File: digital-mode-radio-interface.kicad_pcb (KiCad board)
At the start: 2 copper layers, 9 parts, among them U1 FE1.1s, U2 CH340E, U3 CRE1S0505S3C, U4 PC817, U5 PC817, U6 PC817, U7 PC817

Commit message: WIP checkin of PCB layout
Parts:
- added C1: 475, Capacitor_SMD:C_0201_0603Metric, F.Cu at (89.9, 87.0)
- added C10: 475, Capacitor_SMD:C_0201_0603Metric, F.Cu at (112.8, 115.8)
- added C11: 100n, Capacitor_SMD:C_0201_0603Metric, F.Cu at (53.4, 96.7)
- added C12: 100n, Capacitor_SMD:C_0201_0603Metric, F.Cu at (69.1, 95.5)
- added C13: 4.7u, Capacitor_SMD:C_0201_0603Metric, F.Cu at (70.7, 104.0)
- added C14: 100n, Capacitor_SMD:C_0201_0603Metric, F.Cu at (71.4, 99.9)
- added C15: 4.7u, Capacitor_SMD:C_0201_0603Metric, F.Cu at (70.0, 107.1)
- added C16: 10uF, Capacitor_SMD:C_0201_0603Metric, F.Cu at (42.0, 100.5)
- added C18: 101, Capacitor_SMD:C_0201_0603Metric, F.Cu at (51.9, 106.9)
- added C19: 100n, Capacitor_SMD:C_0201_0603Metric, F.Cu at (69.1, 97.6)
- added C2: 10uF, Capacitor_SMD:C_0201_0603Metric, F.Cu at (89.9, 88.5)
- added C3: 10uF, Capacitor_SMD:C_0201_0603Metric, F.Cu at (55.8, 91.7)
- added C4: 10uF, Capacitor_SMD:C_0201_0603Metric, F.Cu at (44.8, 99.0)
- added C5: 475, Capacitor_SMD:C_0201_0603Metric, F.Cu at (40.7, 87.7)
- added C6: 475, Capacitor_SMD:C_0201_0603Metric, F.Cu at (86.5, 113.2)
- added C7: 10uF, Capacitor_SMD:C_0201_0603Metric, F.Cu at (96.3, 117.3)
- added C8: 475, Capacitor_SMD:C_0201_0603Metric, F.Cu at (125.6, 109.8)
- added C9: 475, Capacitor_SMD:C_0201_0603Metric, F.Cu at (121.8, 118.6)
- added D3: YELLOW, LED_SMD:LED_0201_0603Metric, F.Cu at (55.5, 111.7)
- added D4: RED, LED_SMD:LED_0201_0603Metric, F.Cu at (80.2, 94.3)
- added D5: LED, LED_SMD:LED_0201_0603Metric, F.Cu at (34.8, 107.0)
- added J1: Conn_01x09_Socket, Connector_Dsub:DSUB-9_Female_Horizontal_P2.77x2.84mm_EdgePinOffset4.94mm_Housed_MountingHolesOffset7.48mm, F.Cu at (133.8, 96.4)
- added J2: Conn_01x02, Connector_PinHeader_1.00mm:PinHeader_1x02_P1.00mm_Vertical, F.Cu at (108.1, 97.5)
- added J3: Conn_01x03_Pin, Connector_PinHeader_1.00mm:PinHeader_1x03_P1.00mm_Vertical, F.Cu at (59.7, 110.0)
- added L1: 10uH, Inductor_SMD:L_CommonModeChoke_Coilcraft_0805USB, F.Cu at (31.7, 94.3)
- added P1: USB_C_Plug, Connector_USB:USB_C_Receptacle_GCT_USB4085, F.Cu at (32.5, 99.0)
- added Q1: Q_NPN_BCE, Package_TO_SOT_SMD:SOT-23-3, F.Cu at (100.0, 99.7)
- added Q2: Q_NPN_BCE, Package_TO_SOT_SMD:SOT-23-3, F.Cu at (102.3, 108.1)
- added Q3: Q_NPN_BCE, Package_TO_SOT_SMD:SOT-23-3, F.Cu at (99.0, 87.4)
- added Q4: Q_NPN_BCE, Package_TO_SOT_SMD:SOT-23-3, F.Cu at (93.7, 112.4)
- added R1: 1K, Resistor_SMD:R_0201_0603Metric, F.Cu at (65.4, 83.7)
- added R10: 47k, Resistor_SMD:R_0201_0603Metric, F.Cu at (89.5, 112.7)
- added R11: 510, Resistor_SMD:R_0201_0603Metric, F.Cu at (86.6, 118.7)
- added R12: 10k, Resistor_SMD:R_0201_0603Metric, F.Cu at (89.7, 108.4)
- added R13: 33k, Resistor_SMD:R_0201_0603Metric, F.Cu at (93.7, 93.9)
- added R14: 10k, Resistor_SMD:R_0201_0603Metric, F.Cu at (93.9, 85.3)
- added R15: 330, Resistor_SMD:R_0201_0603Metric, F.Cu at (55.8, 108.8)
- added R16: 330, Resistor_SMD:R_0201_0603Metric, F.Cu at (80.2, 95.5)
- added R17: 22, Resistor_SMD:R_0201_0603Metric, F.Cu at (53.0, 93.1)
- added R18: 22, Resistor_SMD:R_0201_0603Metric, F.Cu at (51.8, 108.2)
- added R19: 2.7k, Resistor_SMD:R_0201_0603Metric, F.Cu at (47.2, 104.7)
- added R2: 1K, Resistor_SMD:R_0201_0603Metric, F.Cu at (35.6, 91.4)
- added R20: 2.7k, Resistor_SMD:R_0201_0603Metric, F.Cu at (34.8, 104.9)
- added R3: 510, Resistor_SMD:R_0201_0603Metric, F.Cu at (46.5, 93.5)
- added R4: 510, Resistor_SMD:R_0201_0603Metric, F.Cu at (59.6, 84.4)
- added R5: 10k, Resistor_SMD:R_0201_0603Metric, F.Cu at (96.3, 87.3)
- added R6: 510, Resistor_SMD:R_0201_0603Metric, F.Cu at (107.1, 84.0)
- added R7: 510, Resistor_SMD:R_0201_0603Metric, F.Cu at (92.7, 90.5)
- added R8: 510, Resistor_SMD:R_0201_0603Metric, F.Cu at (98.6, 106.5)
- added R9: 10K, Resistor_SMD:R_0201_0603Metric, F.Cu at (98.9, 107.8)
- added RV1: 10k, Potentiometer_SMD:Potentiometer_ACP_CA6-VSMD_Vertical, F.Cu at (118.3, 109.8)
- added RV2: 10k, Potentiometer_SMD:Potentiometer_ACP_CA6-VSMD_Vertical, F.Cu at (105.4, 115.8)
- added U8: CM108AH, Package_QFP:LQFP-48_7x7mm_P0.5mm, F.Cu at (63.3, 101.7)
- added U9: 93C46, Package_SO:SOIC-8_3.9x4.9mm_P1.27mm, F.Cu at (53.3, 101.7)
- added Y1: 12MHz, Crystal:Crystal_SMD_FOX_FE-2Pin_7.5x5.0mm_HandSoldering, F.Cu at (35.2, 114.6)
- D1: renamed from D2; footprint Diode_THT:D_DO-35_SOD27_P7.62mm_Horizontal -> Diode_SMD:D_0603_1608Metric
- D2: renamed from D1; footprint Diode_THT:D_DO-35_SOD27_P7.62mm_Horizontal -> Diode_SMD:D_0603_1608Metric
- moved U7 68.1 mm to (41.3, 104.7), turned to 90 degrees
- moved U6 67.5 mm to (40.6, 90.6), turned to 180 degrees
- moved D2 35.8 mm to (107.3, 103.1), turned to 180 degrees
- moved U5 31.3 mm to (79.2, 87.9), turned to 90 degrees
- moved U4 27.8 mm to (73.4, 117.2), turned to 180 degrees
- moved U3 24.1 mm to (69.5, 91.5), turned to 90 degrees
- moved U1 23.7 mm to (77.2, 107.4)
- moved U2 21.9 mm to (77.2, 98.8)
- moved D1 19.2 mm to (105.0, 88.5), turned to 180 degrees
- renumbered U6 to U1, U5 to U2, U4 to U3, U7 to U4, U3 to U5, U2 to U6, U1 to U7
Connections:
- U7 pad 1: unconnected-(U1-VSS-Pad1) -> GNDD
- U7 pad 14: unconnected-(U1-REXT-Pad14) -> Net-(U7-REXT)
- U7 pad 17: unconnected-(U1-~{XRSTJ}-Pad17) -> +3.3VDAC
- U7 pad 18: unconnected-(U1-VBUSM-Pad18) -> +5VD
- U7 pad 19: unconnected-(U1-BUSJ-Pad19) -> GNDD
- U7 pad 2: unconnected-(U1-XOUT-Pad2) -> Net-(U7-XOUT)
- U7 pad 21: unconnected-(U1-VD33_O-Pad21) -> Net-(U7-VD33_O)
- U7 pad 22: unconnected-(U1-DRV-Pad22) -> Net-(U7-DRV)
- U7 pad 3: unconnected-(U1-XIN-Pad3) -> Net-(U7-XIN)
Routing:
- net GNDD: track 0.00 -> 132.7 mm, vias 0 -> 11
- net +5VD: track 0.00 -> 108.9 mm, vias 0 -> 6
- net GND: track 0.00 -> 79.3 mm, vias 0 -> 5
- net Audio Out: track 0.00 -> 64.6 mm, vias 0 -> 2
- net Net-(J1-Pin_4): track 0.00 -> 62.8 mm
- net +5V: track 0.00 -> 53.7 mm
- net Net-(D1-K): track 0.00 -> 50.2 mm, vias 0 -> 1
- net Net-(D2-A): track 0.00 -> 49.7 mm
- net RXD: track 0.00 -> 46.1 mm, vias 0 -> 1
- net +3.3VDAC: track 0.00 -> 41.7 mm
- net Net-(R3-Pad2): track 0.00 -> 39.7 mm, vias 0 -> 2
- net Net-(J1-Pin_3): track 0.00 -> 38.6 mm
- net Audio IN: track 0.00 -> 38.3 mm, vias 0 -> 2
- net Net-(J1-Pin_2): track 0.00 -> 37.4 mm, vias 0 -> 1
- net USB1-: track 0.00 -> 34.6 mm, vias 0 -> 2
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- added copper zone on B.Cu, net GND
- added copper zone on B.Cu, net GNDD
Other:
- board outline added: 115 x 40.6 mm

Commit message: Place Audio tranformers and cleanup routing.    Re-annotate based on geographical layout.
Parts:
- added T1: SM-LP-5001E, Project_Library:RES6_SM-LP-5001E_BRN-L, F.Cu at (105.8, 116.3)
- added T2: SM-LP-5001E, Project_Library:RES6_SM-LP-5001E_BRN-L, F.Cu at (105.8, 106.6)
- moved C13 24.6 mm to (97.8, 113.5), turned to -90 degrees
- moved RV1 14.8 mm to (120.2, 116.1)
- moved C17 14.2 mm to (127.0, 116.1)
- moved D5 14.1 mm to (98.5, 92.0)
- moved C14 13.3 mm to (97.6, 104.0)
- moved J2 13.3 mm to (107.1, 84.3)
- moved Q4 13.3 mm to (99.1, 86.5)
- moved R16 12.7 mm to (112.2, 95.6)
- moved Q3 10.8 mm to (93.1, 102.5)
- moved R15 10.8 mm to (89.7, 102.2)
- moved R18 10.8 mm to (89.4, 100.9)
- moved D4 9.80 mm to (108.3, 97.8)
- moved Q2 9.80 mm to (102.3, 96.6)
- moved R12 9.61 mm to (99.5, 96.3)
- moved C10 4.15 mm to (65.7, 95.1), turned to 180 degrees
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- renumbered C11 to C1, C19 to C10, C14 to C11, C6 to C12, C9 to C13, C7 to C14, C1 to C15, C2 to C16, C10 to C17, C8 to C18, C3 to C2, C16 to C3, C18 to C4, C4 to C5, C5 to C6, C13 to C7, C15 to C8, C12 to C9, D5 to D1, D3 to D2, D4 to D3, D1 to D4, D2 to D5, J3 to J1, J1 to J3, Q4 to Q1, Q3 to Q2, Q2 to Q3, Q1 to Q4, R20 to R1, R16 to R10, R1 to R11, R5 to R12, R12 to R13, R13 to R14, R9 to R15, R6 to R16, R7 to R17, R8 to R18, R10 to R19, R14 to R20, R18 to R3, R19 to R4, R15 to R5, R3 to R6, R17 to R7, R4 to R8, R11 to R9, RV2 to RV1, RV1 to RV2, U7 to U1, U8 to U2, U9 to U3, U6 to U4, U4 to U5, U2 to U6, U3 to U7, U1 to U8, U5 to U9
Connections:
- RV1 pad 3: (no net) -> GND
- RV2 pad 3: (no net) -> GND
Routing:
- net GND: track 79.3 -> 107.8 mm, vias 5 -> 133
- net Net-(D1-K): track 50.2 -> 28.8 mm, vias 1 -> 0
- net Net-(J1-Pin_2): track 37.4 -> 22.8 mm, vias 1 -> 0
- net Net-(D2-A): track 49.7 -> 36.4 mm
- net Net-(Q1-B): track 32.9 -> 21.1 mm, vias 2 -> 1
- net AF OUT: track 33.2 -> 22.7 mm
- net Net-(R8-Pad1): track 21.6 -> 11.8 mm
- net Audio IN: track 38.3 -> 47.8 mm, vias 2 -> 4
- net Audio Out: track 64.6 -> 56.6 mm, vias 2 -> 0
- net Net-(D2-K): track 28.5 -> 36.3 mm
- net GNDD: track 132.7 -> 139.4 mm, vias 11 -> 147
- net Net-(J1-Pin_3): track 38.6 -> 44.5 mm, vias 0 -> 2
- net Net-(RV2-Pad1): track 0.00 -> 4.53 mm
- net Net-(RV1-Pad1): track 0.00 -> 4.32 mm
- net Net-(D1-A): track 12.4 -> 16.6 mm
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- added copper zone on F.Cu, net GND
- added copper zone on F.Cu, net GNDD

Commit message: Move Radio interface onto it's own sheet, Add mounting holes and case outline
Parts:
- added H1: MountingHole, MountingHole:MountingHole_3.2mm_M3, F.Cu at (30.6, 118.1)
- added H2: MountingHole, MountingHole:MountingHole_3.2mm_M3, F.Cu at (30.6, 85.9)
- added H3: MountingHole, MountingHole:MountingHole_3.2mm_M3, F.Cu at (126.9, 118.1)
- added H4: MountingHole, MountingHole:MountingHole_3.2mm_M3, F.Cu at (126.9, 85.9)
- moved Y1 5.35 mm to (40.3, 112.8)
- moved C17 4.81 mm to (126.7, 111.3)
- moved RV1 4.81 mm to (119.9, 111.3)
- moved C18 4.06 mm to (127.0, 102.7)
- moved RV2 4.06 mm to (120.2, 102.7)
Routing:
- net GND: track 107.8 -> 100.4 mm, vias 133 -> 5
- net AF OUT: track 22.7 -> 17.7 mm
- net Net-(U1-XOUT): track 11.0 -> 6.08 mm
- net Net-(RV1-Pad1): track 4.53 -> 7.12 mm
- net Net-(RV2-Pad1): track 4.32 -> 5.99 mm
- net Net-(U1-XIN): track 7.56 -> 9.08 mm
- net GNDD: vias 147 -> 24

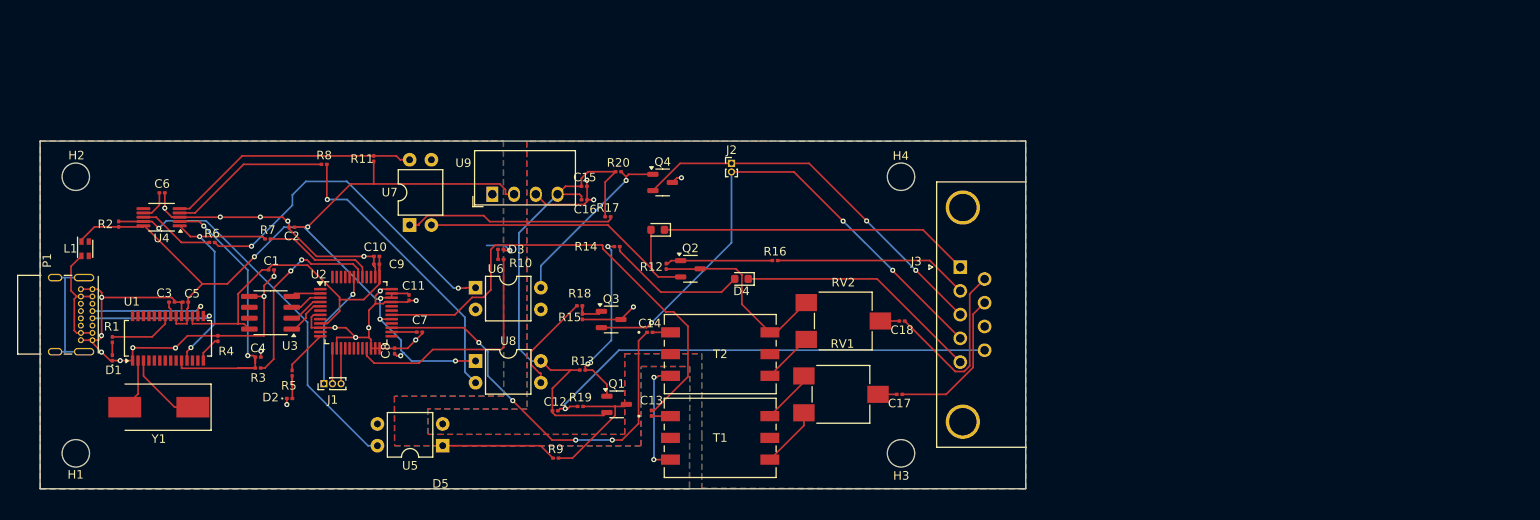
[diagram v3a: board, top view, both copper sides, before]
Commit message: Refresh with kicad 8.0.8
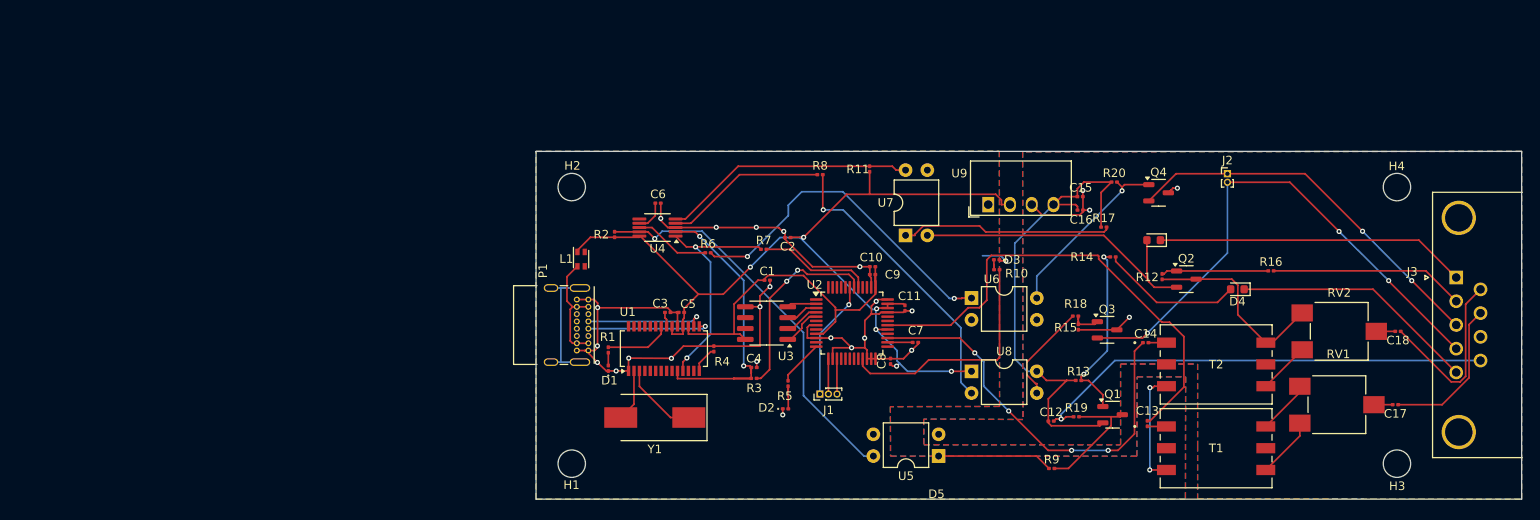
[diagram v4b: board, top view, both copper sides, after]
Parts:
- moved C12 57.9 mm to (144.4, 114.4)
- moved H3 57.9 mm to (184.8, 119.3)
- moved H4 57.9 mm to (184.8, 87.1)
- moved C10 57.9 mm to (123.6, 96.4)
- moved C11 57.9 mm to (127.4, 101.2)
- moved C13 57.9 mm to (155.6, 114.7)
- moved C15 57.9 mm to (147.8, 88.2)
- moved C16 57.9 mm to (147.8, 89.8)
- moved C2 57.9 mm to (113.7, 93.0)
- moved C3 57.9 mm to (99.7, 101.7)
- moved C4 57.9 mm to (109.7, 108.1)
- moved C5 57.9 mm to (101.3, 101.7)
- moved C7 57.9 mm to (128.6, 105.2)
- moved C8 57.9 mm to (125.7, 107.4)
- moved C9 57.9 mm to (123.6, 97.3)
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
